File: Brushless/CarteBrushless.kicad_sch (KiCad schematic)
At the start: 69 parts, among them J16 ALIM, Q2 IRF7424, U1 STM32G484RETx

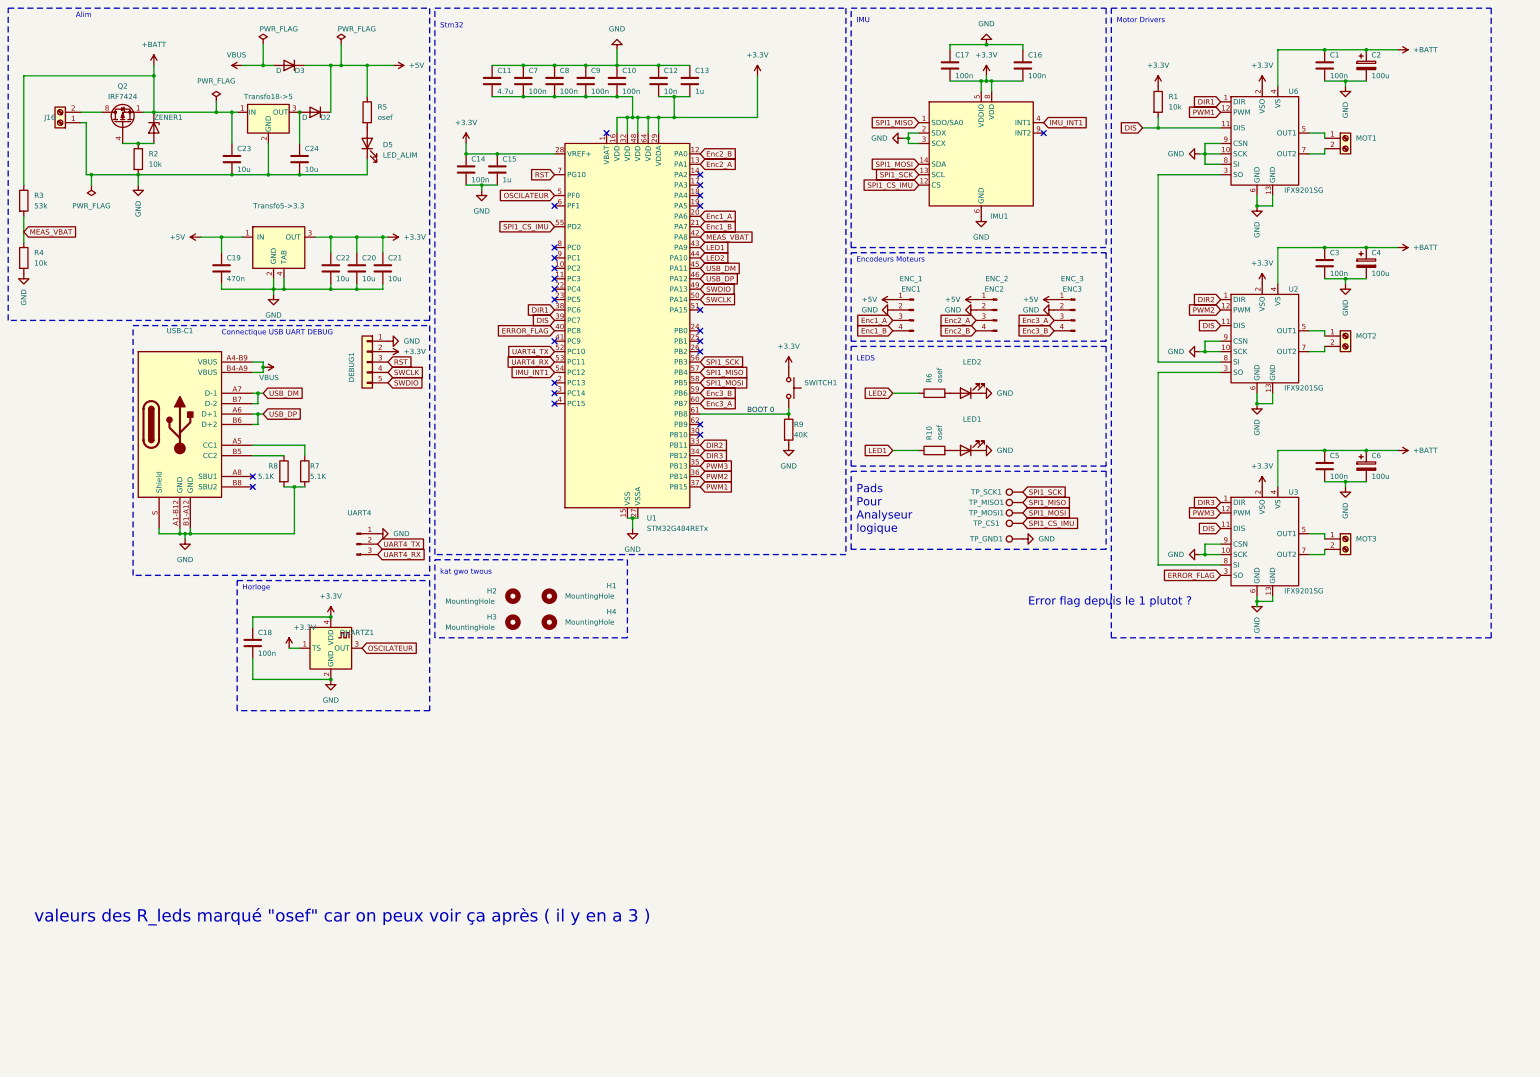
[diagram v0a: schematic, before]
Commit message: Schematic Brushless
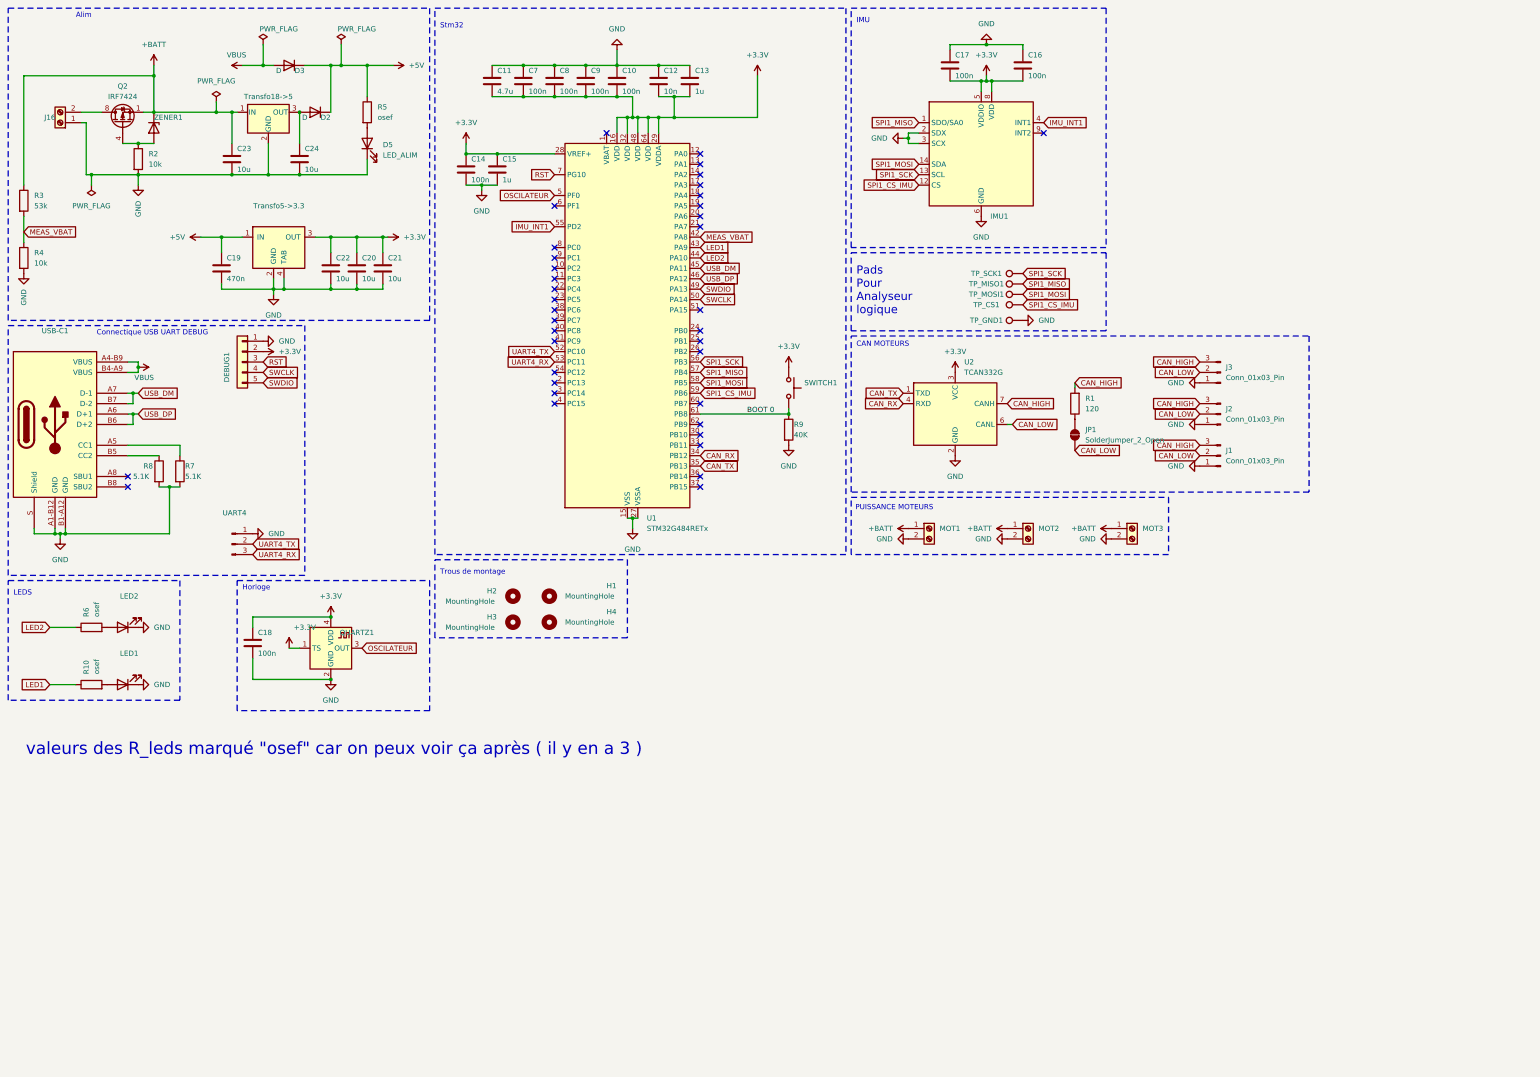
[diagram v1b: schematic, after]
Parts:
- removed C1, C3, C5: 100n, Capacitor_SMD:C_0603_1608Metric, symbol Device:C
- removed C2, C4, C6: 100u, Capacitor_SMD:CP_Elec_10x12.5, symbol Device:C_Polarized
- removed ENC_1: ENC1, Connector_PinHeader_2.54mm:PinHeader_1x04_P2.54mm_Vertical, symbol Connector:Conn_01x04_Pin
- removed ENC_2: ENC2, Connector_PinHeader_2.54mm:PinHeader_1x04_P2.54mm_Vertical, symbol Connector:Conn_01x04_Pin
- removed ENC_3: ENC3, Connector_PinHeader_2.54mm:PinHeader_1x04_P2.54mm_Vertical, symbol Connector:Conn_01x04_Pin
- removed U2, U3, U6: ~, ENAC_robotique:IFX9201SG, symbol ENAC_robotique:IFX9201SG
- added J1, J2, J3: Conn_01x03_Pin, symbol Connector:Conn_01x03_Pin
- added JP1: SolderJumper_2_Open, symbol Jumper:SolderJumper_2_Open
- added U2: TCAN332G, Package_TO_SOT_SMD:SOT-23-8, symbol Interface_CAN_LIN:TCAN332G
- MOT1: value MOT1 -> MOT3; footprint TerminalBlock:TerminalBlock_bornier-2_P5.08mm -> Connector_AMASS:AMASS_XT30UPB-F_1x02_P5.0mm_Vertical
- MOT2: value MOT2 -> MOT3; footprint TerminalBlock:TerminalBlock_bornier-2_P5.08mm -> Connector_AMASS:AMASS_XT30UPB-F_1x02_P5.0mm_Vertical
- MOT3: footprint TerminalBlock:TerminalBlock_bornier-2_P5.08mm -> Connector_AMASS:AMASS_XT30UPB-F_1x02_P5.0mm_Vertical
- R1: value 10k -> 120
- TP_CS1, TP_GND1, TP_MISO1, TP_MOSI1, TP_SCK1: footprint TestPoint:TestPoint_Pad_D2.0mm -> TestPoint:TestPoint_Pad_D1.5mm
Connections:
- net Enc3_B is gone; now on net SPI1_CS_IMU: U1.59 (PB6)
- net +3.3V: now also U2.3 (VCC); no longer R1.1
- net +BATT: now also MOT1.1 (Pin_1), MOT2.1 (Pin_1), MOT3.1 (Pin_1)
- net GND: now also MOT1.2 (Pin_2), MOT2.2 (Pin_2), MOT3.2 (Pin_2), J1.1 (Pin_1), J2.1 (Pin_1), J3.1 (Pin_1), U2.2 (GND)
- net IMU_INT1: now also U1.55 (PD2); no longer U1.54 (PC12)
- net SPI1_CS_IMU: no longer U1.55 (PD2)
- net DIR1: no longer names the net of U1.38 (PC6)
- net DIR2: no longer names the net of U1.33 (PB11)
- net DIR3 renamed CAN_RX
- net CAN_RX: now also U2.4 (RXD)
- net DIS: no longer names the net of U1.39 (PC7)
- net DIS: no longer R1.2
- net ERROR_FLAG: no longer names the net of U1.40 (PC8)
- net Enc1_A: no longer names the net of U1.20 (PA6)
- net Enc1_B: no longer names the net of U1.21 (PA7)
- net Enc2_A: no longer names the net of U1.13 (PA1)
- net Enc2_B: no longer names the net of U1.12 (PA0)
- net Enc3_A: no longer names the net of U1.60 (PB7)
- net PWM1: no longer names the net of U1.37 (PB15)
- net PWM2: no longer names the net of U1.36 (PB14)
- net PWM3 renamed CAN_TX
- net CAN_TX: now also U2.1 (TXD)
- new net: JP1.2 (B), R1.1
- new net CAN_HIGH: J1.3 (Pin_3), J2.3 (Pin_3), J3.3 (Pin_3), R1.2, U2.7 (CANH)
- new net CAN_LOW: J1.2 (Pin_2), J2.2 (Pin_2), J3.2 (Pin_2), JP1.1 (A), U2.6 (CANL)
- no-connect marks 25 -> 37
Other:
- note added: "CAN MOTEURS"
- note added: "PUISSANCE MOTEURS"
- note added: "Trous de montage"
- note removed: "Encodeurs Moteurs"
- note removed: "Error flag depuis le 1 plutot ?"
- note removed: "Motor Drivers"
- note removed: "kat gwo twous"
- moved on the sheet: DEBUG1, LED1, LED2, R10, R6, R7, R8, TP_CS1, TP_GND1, TP_MISO1, TP_MOSI1, TP_SCK1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

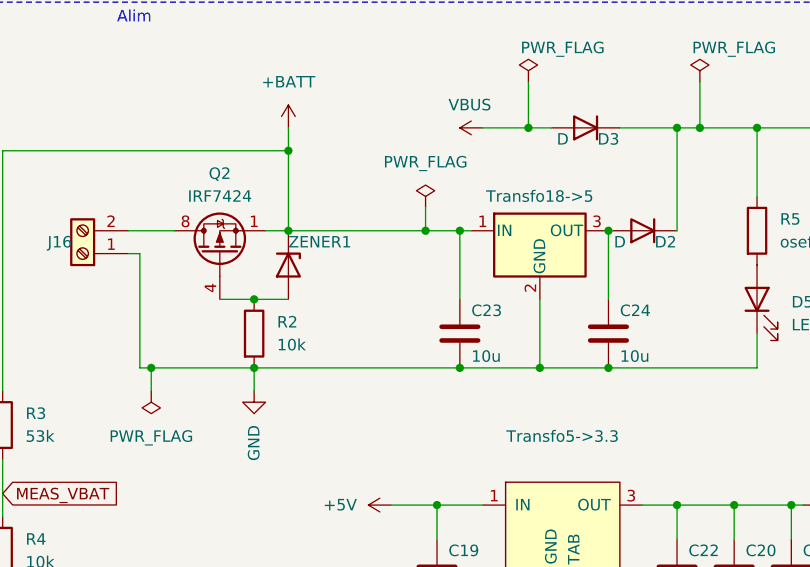
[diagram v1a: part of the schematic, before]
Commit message: tentative de fix du bug de reset
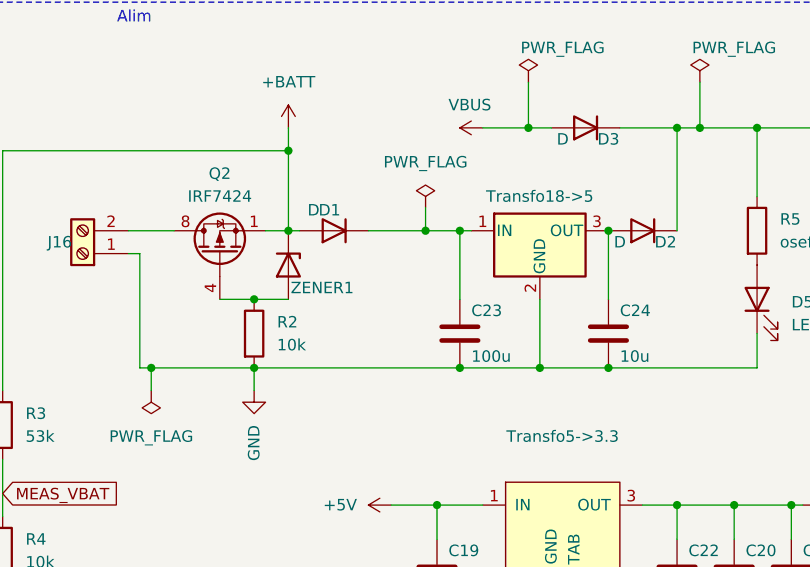
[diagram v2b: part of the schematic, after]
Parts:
- added D1: D, Diode_SMD:Nexperia_CFP3_SOD-123W, symbol Device:D
- C23: value 10u -> 100u; footprint Capacitor_SMD:C_0603_1608Metric -> Capacitor_Tantalum_SMD:CP_EIA-7343-31_Kemet-D_Pad2.25x2.55mm_HandSolder; RS https://fr.rs-online.com/web/p/condensateurs-ceramique-mult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 -> https://fr.rs-online.com/web/p/condensateurs-tantale/135988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
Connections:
- net +BATT: now also D1.2 (A); no longer C23.1, Transfo18->5.1 (IN)
- new net: C23.1, D1.1 (K), Transfo18->5.1 (IN)
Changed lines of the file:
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@@
 	)
 	(junction
-		(at 66.04 44.45)
-		(diameter 0)
-		(color 0 0 0 0)
-	)
-	(junction
 		(at 163.83 33.02)
 		(diameter 0)
@@
 	)
 	(junction
+		(at 66.04 44.45)
+		(diameter 0)
+		(color 0 0 0 0)
+	)
+	(junction
 		(at 140.97 33.02)
 		(diameter 0)
@@
 	(wire
 		(pts
-			(xy 46.99 105.41) (xy 46.99 106.68)
+			(xy 50.8 44.45) (xy 52.07 44.45)
 		)
 		(stroke
@@
 	(wire
 		(pts
-			(xy 252.73 39.37) (xy 252.73 36.83)
+			(xy 46.99 105.41) (xy 46.99 106.68)
 		)
 		(stroke
@@
 	(wire
 		(pts
-			(xy 66.04 44.45) (xy 69.85 44.45)
+			(xy 252.73 39.37) (xy 252.73 36.83)
 		)
 		(stroke
@@
 	(wire
 		(pts
-			(xy 50.8 44.45) (xy 66.04 44.45)
+			(xy 66.04 44.45) (xy 69.85 44.45)
 		)
 		(stroke
@@
 	(wire
 		(pts
+			(xy 59.69 44.45) (xy 66.04 44.45)
+		)
+		(stroke
+			(width 0)
+			(type default)
+		)
+	)
+	(wire
+		(pts
 			(xy 67.31 87.63) (xy 80.01 87.63)
 		)
@@
 			)
 		)
-		(property "Value" "10u"
+		(property "Value" "100u"
 			(at 71.12 58.42 0)
 			(effects
@@
 			)
 		)
-		(property "Footprint" "Capacitor_SMD:C_0603_1608Metric"
+		(property "Footprint" "Capacitor_Tantalum_SMD:CP_EIA-7343-31_Kemet-D_Pad2.25x2.55mm_HandSolder"
 			(at 70.8152 59.69 0)
 			(effects
@@
 			)
 		)
-		(property "Datasheet" "https://docs.rs-online.com/601e/0900766b81110dfe.pdf"
+		(property "Datasheet" "https://docs.rs-online.com/5541/0900766b815b82a1.pdf"
 			(at 69.85 55.88 0)
 			(effects
@@
 			)
 		)
-		(property "RS" "https://fr.rs-online.com/web/p/condensateurs-ceramique-multicouches/7661104"
+		(property "RS" "https://fr.rs-online.com/web/p/condensateurs-tantale/1359884?searchId=5f999e37-8b6c-46c8-85bd-4dcc7cb65396&gb=s"
 			(at 69.85 55.88 0)
 			(effects
@@
 		(dnp no)
 		(property "Reference" "ZENER1"
-			(at 50.8 45.72 90)
+			(at 51.054 50.8 90)
 			(effects
 				(font
@@
 					(unit 1)
 				)
+			)
+		)
+	)
+	(symbol
+		(lib_id "Device:D")
+		(at 55.88 44.45 180)
+		(unit 1)
+		(exclude_from_sim no)
+		(in_bom yes)
+		(on_board yes)
+		(dnp no)
+		(property "Reference" "D1"
+			(at 55.372 42.164 0)
+			(effects
+				(font
+					(size 1.27 1.27)
+				)
+			)
+		)
+		(property "Value" "D"
+			(at 53.594 42.164 0)
+			(effects
+				(font
+					(size 1.27 1.27)
+				)
+			)
+		)
+		(property "Footprint" "Diode_SMD:Nexperia_CFP3_SOD-123W"
+			(at 55.88 44.45 0)
+			(effects
+				(font
+					(size 1.27 1.27)
+				)
+				(hide yes)
+			)
+		)
+		(property "Datasheet" "~"
+			(at 55.88 44.45 0)
+			(effects
+				(font
+					(size 1.27 1.27)
+				)
+				(hide yes)
+			)
+		)
+		(property "Description" ""
+			(at 55.88 44.45 0)
+			(effects
+				(font
+					(size 1.27 1.27)
+				)
+				(hide yes)
+			)
+		)
+		(property "Sim.Device" "D"
+			(at 55.88 44.45 0)
+			(effects
+				(font
+					(size 1.27 1.27)
+				)
+				(hide yes)
+			)
+		)
+		(property "Sim.Pins" "1=K 2=A"
+			(at 55.88 44.45 0)
+			(effects
+				(font
+					(size 1.27 1.27)
+				)
+				(hide yes)
+			)
+		)
+		(pin "1"
+		)
+		(pin "2"
+		)
+		(instances
+			(project "CarteBrushless"
+				(path "/f941aee9-3a44-439b-9c30-032c53e86031"
+					(reference "D1")
+					(unit 1)
+				)

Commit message: placement PCB
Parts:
- added JP2: SolderJumper_2_Open, Jumper:SolderJumper-2_P1.3mm_Open_RoundedPad1.0x1.5mm, symbol Jumper:SolderJumper_2_Open
- added R11: 120, Resistor_SMD:R_0805_2012Metric, symbol Device:R
- J1, J2, J3: footprint (none) -> Connector_Molex:Molex_PicoBlade_53398-0371_1x03-1MP_P1.25mm_Vertical
- JP1: footprint (none) -> Jumper:SolderJumper-2_P1.3mm_Open_RoundedPad1.0x1.5mm
- UART1: renamed from UART4; footprint Connector_PinHeader_2.54mm:PinHeader_1x03_P2.54mm_Vertical -> Connector_Molex:Molex_PicoBlade_53398-0371_1x03-1MP_P1.25mm_Vertical
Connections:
- net +BATT: now also MOT1.2 (Pin_2), MOT2.2 (Pin_2), MOT3.2 (Pin_2); no longer MOT1.1 (Pin_1), MOT2.1 (Pin_1), MOT3.1 (Pin_1)
- net CAN_HIGH: now also JP2.2 (B)
- net CAN_LOW: now also R11.1
- net GND: now also MOT1.1 (Pin_1), MOT2.1 (Pin_1), MOT3.1 (Pin_1); no longer MOT1.2 (Pin_2), MOT2.2 (Pin_2), MOT3.2 (Pin_2)
- net LED1: now also U1.9 (PC1); no longer U1.43 (PA9)
- net LED2: now also U1.10 (PC2); no longer U1.44 (PA10)
- net MEAS_VBAT: now also U1.18 (PA4); no longer U1.42 (PA8)
- net UART2_TX: now reaches U1.14 (PA2)
- net UART2_TX: now also UART1.2 (Pin_2)
- net UART2_RX: now reaches U1.17 (PA3)
- net UART2_RX: now also UART1.3 (Pin_3)
- net UART4_RX: no longer names the net of U1.53 (PC11)
- net UART4_RX: no longer UART1.3 (Pin_3)
- net UART4_TX: no longer names the net of U1.52 (PC10)
- net UART4_TX: no longer UART1.2 (Pin_2)
- new net: JP2.1 (A), R11.2
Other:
- note added: "VERIFIER l'ORDRE DES PINS DES MOLEX et les valeurs de resistances de terminaison"
- moved on the sheet: JP1, R1

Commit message: Routage fini
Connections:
- net +3.3V: now also DEBUG1.4 (Pin_4); no longer DEBUG1.2 (Pin_2)
- net GND: now also DEBUG1.5 (Pin_5); no longer DEBUG1.1 (Pin_1)
- net SWCLK: now also DEBUG1.2 (Pin_2); no longer DEBUG1.4 (Pin_4)
- net SWDIO: now also DEBUG1.1 (Pin_1); no longer DEBUG1.5 (Pin_5)
- net UART2_RX: now also UART1.2 (Pin_2); no longer UART1.3 (Pin_3)
- net UART2_TX: now also UART1.3 (Pin_3); no longer UART1.2 (Pin_2)
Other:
- note added: "(MARGA-RET)"
- note added: "- Check ! - Check !"
- note added: "ALIMENTATION"
- note added: "HORLOGE"
- note added: "Pads Pour Analyseur Logique"
- note added: "R terminaison"
- note added: "STM32"
- note added: "VERIFIER: - l'ordre des pins de molex - Les valeurs de resistances de terminaison"
- note added: "Valeurs des R_leds marqué "osef" (il y en a 3 ) Elles sont reliées à des leds donc on peut les choisir après"
- note added: "connecteurs des drivers moteurs"
- note removed: "Alim"
- note removed: "Horloge"
- note removed: "Pads Pour Analyseur logique"
- note removed: "Stm32"
- note removed: "VERIFIER l'ORDRE DES PINS DES MOLEX et les valeurs de resistances de terminaison"
- note removed: "valeurs des R_leds marqué "osef" car on peux voir ça après ( il y en a 3 )"
- moved on the sheet: C18, H1, H2, H3, H4, QUARTZ1

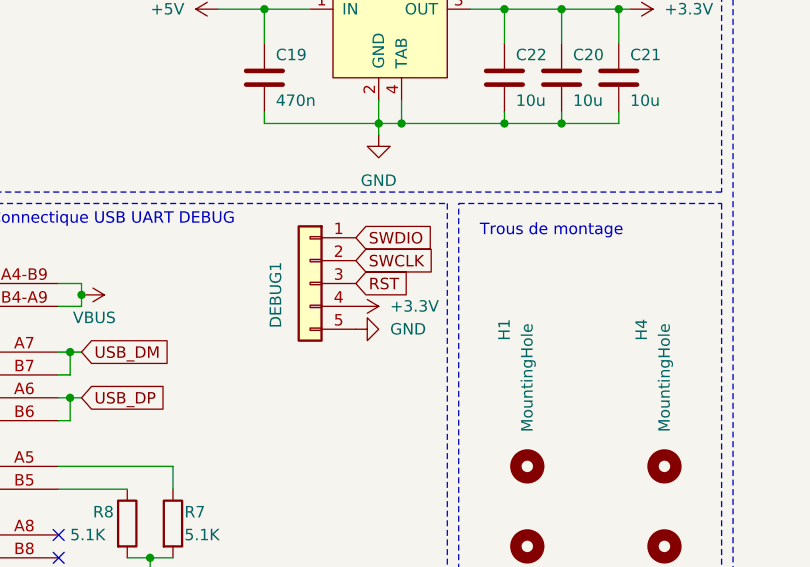
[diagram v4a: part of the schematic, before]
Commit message: change SWD footprint
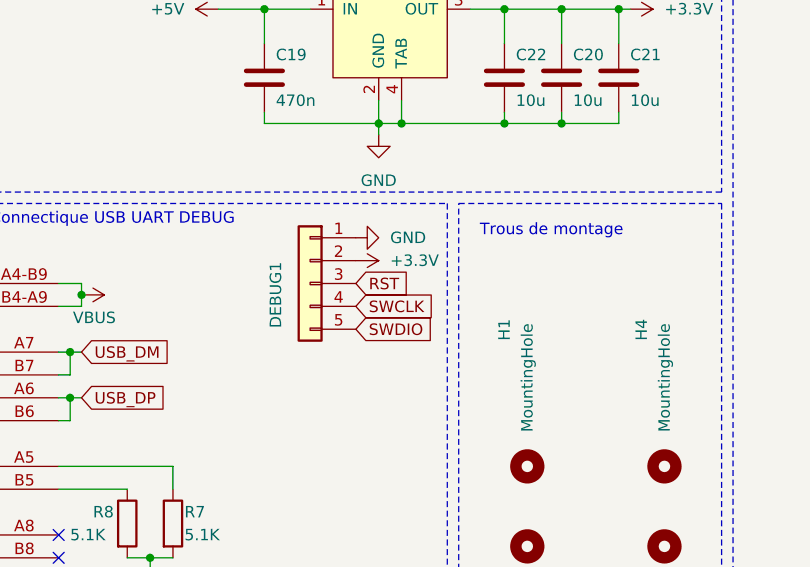
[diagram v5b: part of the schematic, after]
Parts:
- DEBUG1: footprint Connector_Molex:Molex_CLIK-Mate_502382-0570_1x05-1MP_P1.25mm_Vertical -> Connector_Molex:Molex_PicoBlade_53398-0571_1x05-1MP_P1.25mm_Vertical
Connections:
- net +3.3V: now also DEBUG1.2 (Pin_2); no longer DEBUG1.4 (Pin_4)
- net GND: now also DEBUG1.1 (Pin_1); no longer DEBUG1.5 (Pin_5)
- net SWCLK: now also DEBUG1.4 (Pin_4); no longer DEBUG1.2 (Pin_2)
- net SWDIO: now also DEBUG1.5 (Pin_5); no longer DEBUG1.1 (Pin_1)
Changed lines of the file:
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@@
 	(global_label "SWDIO"
 		(shape input)
-		(at 77.47 100.33 0)
+		(at 77.47 110.49 0)
 		(fields_autoplaced yes)
 		(effects
@@
 		)
 		(property "Intersheetrefs" "${INTERSHEET_REFS}"
-			(at 86.3214 100.33 0)
+			(at 86.3214 110.49 0)
 			(effects
 				(font
@@
 	(global_label "SWCLK"
 		(shape input)
-		(at 77.47 102.87 0)
+		(at 77.47 107.95 0)
 		(fields_autoplaced yes)
 		(effects
@@
 		)
 		(property "Intersheetrefs" "${INTERSHEET_REFS}"
-			(at 86.6842 102.87 0)
+			(at 86.6842 107.95 0)
 			(effects
 				(font
@@
 	(symbol
 		(lib_id "power:GND")
-		(at 77.47 110.49 90)
+		(at 77.47 100.33 90)
 		(mirror x)
 		(unit 1)
@@
 		(fields_autoplaced yes)
 		(property "Reference" "#PWR030"
-			(at 83.82 110.49 0)
+			(at 83.82 100.33 0)
 			(effects
 				(font
@@
 		)
 		(property "Value" "GND"
-			(at 81.28 110.49 90)
+			(at 81.28 100.33 90)
 			(effects
 				(font
@@
 		)
 		(property "Footprint" ""
-			(at 77.47 110.49 0)
+			(at 77.47 100.33 0)
 			(effects
 				(font
@@
 		)
 		(property "Datasheet" ""
-			(at 77.47 110.49 0)
+			(at 77.47 100.33 0)
 			(effects
 				(font
@@
 		)
 		(property "Description" ""
-			(at 77.47 110.49 0)
+			(at 77.47 100.33 0)
 			(effects
 				(font
@@
 	(symbol
 		(lib_id "power:+3.3V")
-		(at 77.47 107.95 270)
+		(at 77.47 102.87 270)
 		(mirror x)
 		(unit 1)
@@
 		(fields_autoplaced yes)
 		(property "Reference" "#PWR031"
-			(at 73.66 107.95 0)
+			(at 73.66 102.87 0)
 			(effects
 				(font
@@
 		)
 		(property "Value" "+3.3V"
-			(at 81.28 107.95 90)
+			(at 81.28 102.87 90)
 			(effects
 				(font
@@
 		)
 		(property "Footprint" ""
-			(at 77.47 107.95 0)
+			(at 77.47 102.87 0)
 			(effects
 				(font
@@
 		)
 		(property "Datasheet" ""
-			(at 77.47 107.95 0)
+			(at 77.47 102.87 0)
 			(effects
 				(font
@@
 		)
 		(property "Description" ""
-			(at 77.47 107.95 0)
+			(at 77.47 102.87 0)
 			(effects
 				(font
@@
 			)
 		)
-		(property "Footprint" "Connector_Molex:Molex_CLIK-Mate_502382-0570_1x05-1MP_P1.25mm_Vertical"
+		(property "Footprint" "Connector_Molex:Molex_PicoBlade_53398-0571_1x05-1MP_P1.25mm_Vertical"
 			(at 72.39 105.41 0)
 			(effects
